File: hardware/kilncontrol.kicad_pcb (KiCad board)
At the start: 2 copper layers, 100 x 100 mm, 4 parts

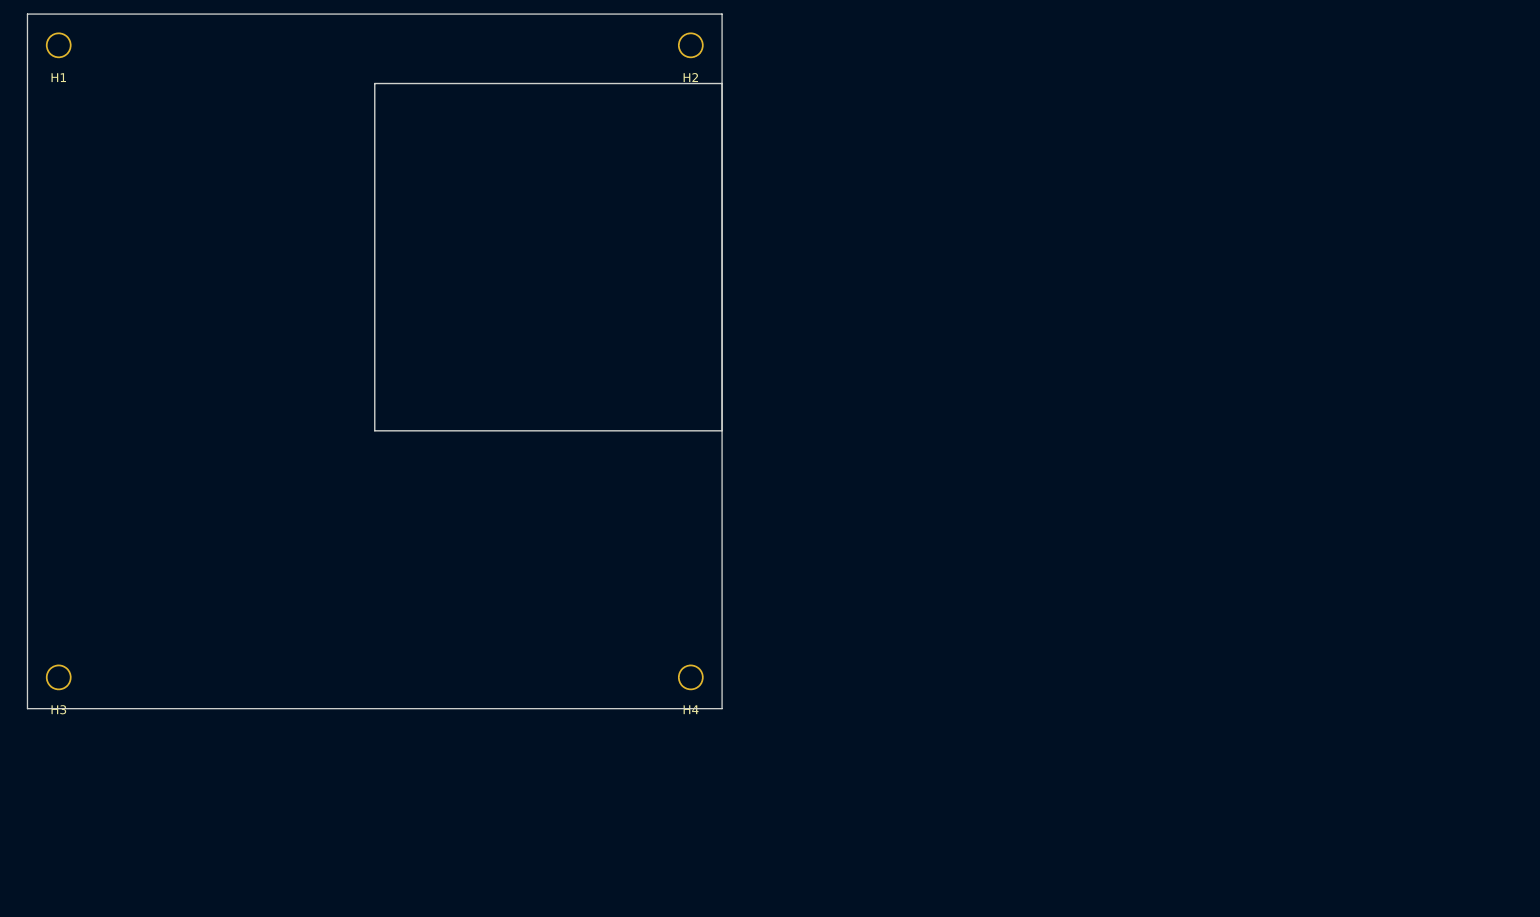
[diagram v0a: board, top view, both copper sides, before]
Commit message: Replace the external buzzer with an on-board one, shrink the test points
Buzzer
  J9, the screw terminal for an external buzzer, is replaced by BZ1 on the
  board: a TMB12A05, 5 V active (self-driving) magnetic buzzer, LCSC C96093.

  Active rather than passive: the 5 V-capable SMD passive part found on LCSC
  is rated 2.5-4.5 V and would be overdriven on the 5 V rail, and an active
  buzzer drops straight into the existing Q4 low-side driver and its flyback
  diode. No circuit change and no firmware change, because SR-20 asks the
  fault and completion alarms to be distinguishable by pattern, not by pitch,
  which kiln_alarm_pattern_t already does.

  This removes the auxiliary-relay output the old terminal also provided. The
  ALARM signal remains available at TP23 if an external annunciator is wanted
  later.

Test points
  All 33 change from TestPoint_THTPad_D2.0mm_Drill1.0mm to
  TestPoint_Pad_1.5x1.5mm: smaller, and SMD, so they sit on the top copper
  layer by construction rather than by layout discipline. The whole board can
  be probed without turning it over, and 33 drilled holes leave the board.

  A note on the sheet tells whoever does the placement not to move any test
  point to the bottom layer.

Requirements
  HR-09 now specifies an on-board buzzer rather than an alarm output capable
  of driving one. SR-20 reworded to match. New HR-19 (test points on the top
  layer only) and HR-20 (small pads, no drilled hole).

Housing
  The lid gains a perforated sound port above BZ1. A buzzer sealed inside the
  box is heavily muffled and SR-20 depends on the operator hearing it; a ring
  of 1.6 mm holes lets the sound out without leaving an opening large enough
  to drop debris onto the board.

Board
  Footprints imported from the schematic in KiCad since the last commit, and
  that import deleted the four M3 mounting holes, which are restored here.

  The imported footprints are STALE: they still carry J9, lack BZ1, and use
  the old 2 mm through-hole test pad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
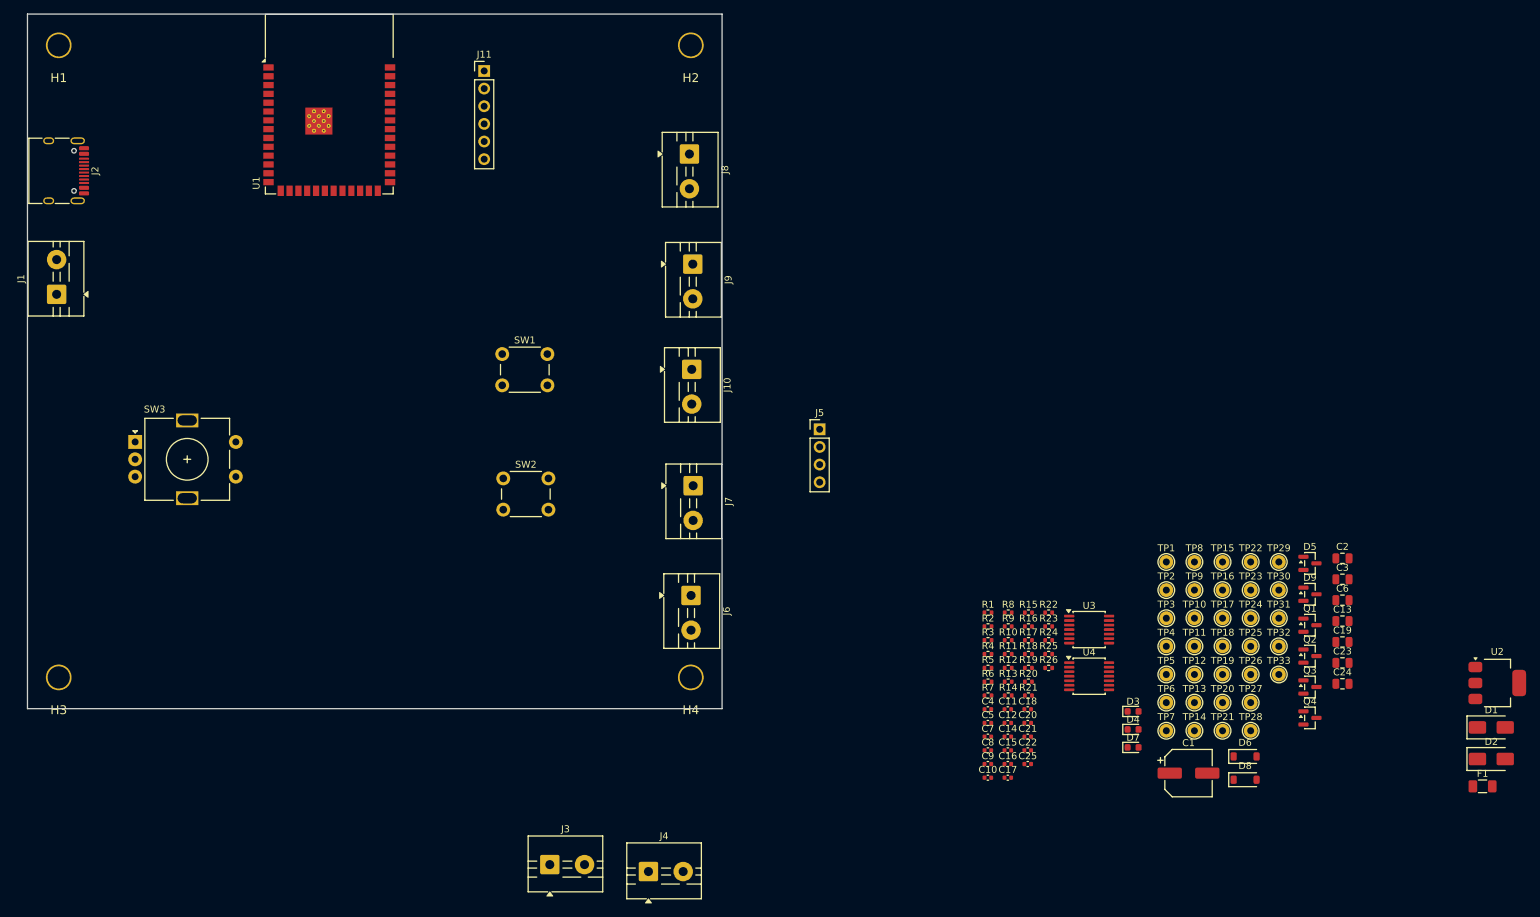
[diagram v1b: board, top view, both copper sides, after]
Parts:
- added C1: 100uF 16V, Capacitor_SMD:CP_Elec_6.3x7.7, F.Cu at (217.2, 149.3)
- added C10: 100pF, Capacitor_SMD:C_0402_1005Metric, F.Cu at (188.3, 149.9)
- added C11: 100nF, Capacitor_SMD:C_0402_1005Metric, F.Cu at (191.1, 140.1)
- added C12: 100nF, Capacitor_SMD:C_0402_1005Metric, F.Cu at (191.1, 142.1)
- added C13: 10uF, Capacitor_SMD:C_0805_2012Metric, F.Cu at (239.3, 127.4)
- added C14: 10nF, Capacitor_SMD:C_0402_1005Metric, F.Cu at (191.1, 144.0)
- added C15: 100pF, Capacitor_SMD:C_0402_1005Metric, F.Cu at (191.1, 146.0)
- added C16: 100pF, Capacitor_SMD:C_0402_1005Metric, F.Cu at (191.1, 148.0)
- added C17: 100nF, Capacitor_SMD:C_0402_1005Metric, F.Cu at (191.1, 149.9)
- added C18: 100nF, Capacitor_SMD:C_0402_1005Metric, F.Cu at (194.0, 140.1)
- added C19: 10uF, Capacitor_SMD:C_0805_2012Metric, F.Cu at (239.3, 130.4)
- added C2: 10uF, Capacitor_SMD:C_0805_2012Metric, F.Cu at (239.3, 118.4)
- added C20: 100nF, Capacitor_SMD:C_0402_1005Metric, F.Cu at (194.0, 142.1)
- added C21: 100nF, Capacitor_SMD:C_0402_1005Metric, F.Cu at (194.0, 144.0)
- added C22: 100nF, Capacitor_SMD:C_0402_1005Metric, F.Cu at (194.0, 146.0)
- added C23: 10uF, Capacitor_SMD:C_0805_2012Metric, F.Cu at (239.3, 133.4)
- added C24: 3.3uF, Capacitor_SMD:C_0805_2012Metric, F.Cu at (239.3, 136.4)
- added C25: 220nF, Capacitor_SMD:C_0402_1005Metric, F.Cu at (194.0, 148.0)
- added C3: 10uF, Capacitor_SMD:C_0805_2012Metric, F.Cu at (239.3, 121.4)
- added C4: 100nF, Capacitor_SMD:C_0402_1005Metric, F.Cu at (188.3, 140.1)
- added C5: 100nF, Capacitor_SMD:C_0402_1005Metric, F.Cu at (188.3, 142.1)
- added C6: 10uF, Capacitor_SMD:C_0805_2012Metric, F.Cu at (239.3, 124.4)
- added C7: 1uF, Capacitor_SMD:C_0402_1005Metric, F.Cu at (188.3, 144.0)
- added C8: 10nF, Capacitor_SMD:C_0402_1005Metric, F.Cu at (188.3, 146.0)
- added C9: 100pF, Capacitor_SMD:C_0402_1005Metric, F.Cu at (188.3, 148.0)
- added D1: SS34, Diode_SMD:D_SMA, F.Cu at (260.8, 142.7)
- added D2: SS34, Diode_SMD:D_SMA, F.Cu at (260.8, 147.2)
- added D3: SSR1, LED_SMD:LED_0603_1608Metric, F.Cu at (209.2, 140.4)
- added D4: SSR2, LED_SMD:LED_0603_1608Metric, F.Cu at (209.2, 143.0)
- added D5: BAT54S, Package_TO_SOT_SMD:SOT-23, F.Cu at (234.6, 119.1)
- added D6: 1N4148W, Diode_SMD:D_SOD-123, F.Cu at (225.3, 146.9)
- added D7: COIL, LED_SMD:LED_0603_1608Metric, F.Cu at (209.2, 145.6)
- added D8: 1N4148W, Diode_SMD:D_SOD-123, F.Cu at (225.3, 150.2)
- added D9: BAT54S, Package_TO_SOT_SMD:SOT-23, F.Cu at (234.6, 123.5)
- added F1: PTC 1.5A, Fuse:Fuse_1206_3216Metric, F.Cu at (259.5, 151.2)
- added J1: 5V DC IN, TerminalBlock:TerminalBlock_MaiXu_MX126-5.0-02P_1x02_P5.00mm, F.Cu at (54.2, 80.3)
- added J10: CT 30A/1V (opt), TerminalBlock:TerminalBlock_MaiXu_MX126-5.0-02P_1x02_P5.00mm, F.Cu at (145.6, 91.2)
- added J11: UART / EXPANSION, Connector_PinHeader_2.54mm:PinHeader_1x06_P2.54mm_Vertical, F.Cu at (115.8, 48.2)
- added J2: USB-C, Connector_USB:USB_C_Receptacle_HRO_TYPE-C-31-M-12, F.Cu at (54.1, 62.6)
- added J3: TC1 KILN (K), TerminalBlock:TerminalBlock_MaiXu_MX126-5.0-02P_1x02_P5.00mm, F.Cu at (125.2, 162.4)
- added J4: TC2 CASE (K), TerminalBlock:TerminalBlock_MaiXu_MX126-5.0-02P_1x02_P5.00mm, F.Cu at (139.4, 163.4)
- added J5: OLED 128x64 I2C, Connector_PinHeader_2.54mm:PinHeader_1x04_P2.54mm_Vertical, F.Cu at (164.1, 99.8)
- added J6: SSR1 CTRL, TerminalBlock:TerminalBlock_MaiXu_MX126-5.0-02P_1x02_P5.00mm, F.Cu at (145.5, 123.7)
- added J7: SSR2 CTRL (opt), TerminalBlock:TerminalBlock_MaiXu_MX126-5.0-02P_1x02_P5.00mm, F.Cu at (145.8, 107.9)
- added J8: CONTACTOR COIL 5V, TerminalBlock:TerminalBlock_MaiXu_MX126-5.0-02P_1x02_P5.00mm, F.Cu at (145.3, 60.1)
- added J9: BUZZER / AUX, TerminalBlock:TerminalBlock_MaiXu_MX126-5.0-02P_1x02_P5.00mm, F.Cu at (145.8, 76.0)
- added Q1: AO3400A, Package_TO_SOT_SMD:SOT-23, F.Cu at (234.6, 128.0)
- added Q2: AO3400A, Package_TO_SOT_SMD:SOT-23, F.Cu at (234.6, 132.4)
- added Q3: AO3400A, Package_TO_SOT_SMD:SOT-23, F.Cu at (234.6, 136.9)
- added Q4: AO3400A, Package_TO_SOT_SMD:SOT-23, F.Cu at (234.6, 141.3)
- added R1: 5.1k, Resistor_SMD:R_0402_1005Metric, F.Cu at (188.3, 126.2)
- added R10: 10k, Resistor_SMD:R_0402_1005Metric, F.Cu at (191.2, 130.2)
- added R11: 10k, Resistor_SMD:R_0402_1005Metric, F.Cu at (191.2, 132.1)
- added R12: 10k, Resistor_SMD:R_0402_1005Metric, F.Cu at (191.2, 134.1)
- added R13: 100R, Resistor_SMD:R_0402_1005Metric, F.Cu at (191.2, 136.1)
- added R14: 10k, Resistor_SMD:R_0402_1005Metric, F.Cu at (191.2, 138.1)
- added R15: 1k, Resistor_SMD:R_0402_1005Metric, F.Cu at (194.1, 126.2)
- added R16: 100R, Resistor_SMD:R_0402_1005Metric, F.Cu at (194.1, 128.2)
- added R17: 10k, Resistor_SMD:R_0402_1005Metric, F.Cu at (194.1, 130.2)
- added R18: 1k, Resistor_SMD:R_0402_1005Metric, F.Cu at (194.1, 132.1)
- added R19: 100R, Resistor_SMD:R_0402_1005Metric, F.Cu at (194.1, 134.1)
- added R2: 5.1k, Resistor_SMD:R_0402_1005Metric, F.Cu at (188.3, 128.2)
- added R20: 47k, Resistor_SMD:R_0402_1005Metric, F.Cu at (194.1, 136.1)
- added R21: 1k, Resistor_SMD:R_0402_1005Metric, F.Cu at (194.1, 138.1)
- added R22: 100R, Resistor_SMD:R_0402_1005Metric, F.Cu at (197.0, 126.2)
- added R23: 10k, Resistor_SMD:R_0402_1005Metric, F.Cu at (197.0, 128.2)
- added R24: 10k, Resistor_SMD:R_0402_1005Metric, F.Cu at (197.0, 130.2)
- added R25: 10k, Resistor_SMD:R_0402_1005Metric, F.Cu at (197.0, 132.1)
- added R26: 1k, Resistor_SMD:R_0402_1005Metric, F.Cu at (197.0, 134.1)
- added R3: 10k, Resistor_SMD:R_0402_1005Metric, F.Cu at (188.3, 130.2)
- added R4: 100R, Resistor_SMD:R_0402_1005Metric, F.Cu at (188.3, 132.1)
- added R5: 100R, Resistor_SMD:R_0402_1005Metric, F.Cu at (188.3, 134.1)
- added R6: 100R, Resistor_SMD:R_0402_1005Metric, F.Cu at (188.3, 136.1)
- added R7: 100R, Resistor_SMD:R_0402_1005Metric, F.Cu at (188.3, 138.1)
- added R8: 4.7k, Resistor_SMD:R_0402_1005Metric, F.Cu at (191.2, 126.2)
- added R9: 4.7k, Resistor_SMD:R_0402_1005Metric, F.Cu at (191.2, 128.2)
- added SW1: RESET, Button_Switch_THT:SW_PUSH_6mm_H5mm, F.Cu at (118.3, 89.0)
- added SW2: BOOT, Button_Switch_THT:SW_PUSH_6mm_H5mm, F.Cu at (118.5, 106.8)
- added SW3: ENCODER, Rotary_Encoder:RotaryEncoder_Alps_EC11E-Switch_Vertical_H20mm, F.Cu at (65.5, 101.6)
- added TP1: +5V, TestPoint:TestPoint_THTPad_D2.0mm_Drill1.0mm, F.Cu at (214.0, 118.9)
- added TP10: TC2_CS, TestPoint:TestPoint_THTPad_D2.0mm_Drill1.0mm, F.Cu at (218.0, 127.0)
- added TP11: TC1_DRDY, TestPoint:TestPoint_THTPad_D2.0mm_Drill1.0mm, F.Cu at (218.0, 131.0)
- added TP12: TC2_DRDY, TestPoint:TestPoint_THTPad_D2.0mm_Drill1.0mm, F.Cu at (218.0, 135.1)
- added TP13: TC1_FAULT, TestPoint:TestPoint_THTPad_D2.0mm_Drill1.0mm, F.Cu at (218.0, 139.1)
- added TP14: TC2_FAULT, TestPoint:TestPoint_THTPad_D2.0mm_Drill1.0mm, F.Cu at (218.0, 143.2)
- added TP15: I2C_SDA, TestPoint:TestPoint_THTPad_D2.0mm_Drill1.0mm, F.Cu at (222.1, 118.9)
- added TP16: I2C_SCL, TestPoint:TestPoint_THTPad_D2.0mm_Drill1.0mm, F.Cu at (222.1, 122.9)
- added TP17: SSR1, TestPoint:TestPoint_THTPad_D2.0mm_Drill1.0mm, F.Cu at (222.1, 127.0)
- added TP18: SSR2, TestPoint:TestPoint_THTPad_D2.0mm_Drill1.0mm, F.Cu at (222.1, 131.0)
- added TP19: HEAT_EN, TestPoint:TestPoint_THTPad_D2.0mm_Drill1.0mm, F.Cu at (222.1, 135.1)
- added TP2: +3V3, TestPoint:TestPoint_THTPad_D2.0mm_Drill1.0mm, F.Cu at (214.0, 122.9)
- added TP20: PUMP_NODE, TestPoint:TestPoint_THTPad_D2.0mm_Drill1.0mm, F.Cu at (222.1, 139.1)
- added TP21: HEAT_EN_DC, TestPoint:TestPoint_THTPad_D2.0mm_Drill1.0mm, F.Cu at (222.1, 143.2)
- added TP22: COIL_DRV, TestPoint:TestPoint_THTPad_D2.0mm_Drill1.0mm, F.Cu at (226.1, 118.9)
- added TP23: ALARM, TestPoint:TestPoint_THTPad_D2.0mm_Drill1.0mm, F.Cu at (226.1, 122.9)
- added TP24: ENC_A, TestPoint:TestPoint_THTPad_D2.0mm_Drill1.0mm, F.Cu at (226.1, 127.0)
- added TP25: ENC_B, TestPoint:TestPoint_THTPad_D2.0mm_Drill1.0mm, F.Cu at (226.1, 131.0)
- added TP26: ENC_BTN, TestPoint:TestPoint_THTPad_D2.0mm_Drill1.0mm, F.Cu at (226.1, 135.1)
- added TP27: TC1_P, TestPoint:TestPoint_THTPad_D2.0mm_Drill1.0mm, F.Cu at (226.1, 139.1)
- added TP28: TC1_N, TestPoint:TestPoint_THTPad_D2.0mm_Drill1.0mm, F.Cu at (226.1, 143.2)
- added TP29: TC2_P, TestPoint:TestPoint_THTPad_D2.0mm_Drill1.0mm, F.Cu at (230.2, 118.9)
- added TP3: GND, TestPoint:TestPoint_THTPad_D2.0mm_Drill1.0mm, F.Cu at (214.0, 127.0)
- added TP30: TC2_N, TestPoint:TestPoint_THTPad_D2.0mm_Drill1.0mm, F.Cu at (230.2, 122.9)
- added TP31: CURR_SENSE, TestPoint:TestPoint_THTPad_D2.0mm_Drill1.0mm, F.Cu at (230.2, 127.0)
- added TP32: MCU_EN, TestPoint:TestPoint_THTPad_D2.0mm_Drill1.0mm, F.Cu at (230.2, 131.0)
- added TP33: MCU_IO0, TestPoint:TestPoint_THTPad_D2.0mm_Drill1.0mm, F.Cu at (230.2, 135.1)
- added TP4: GND, TestPoint:TestPoint_THTPad_D2.0mm_Drill1.0mm, F.Cu at (214.0, 131.0)
- added TP5: VBUS, TestPoint:TestPoint_THTPad_D2.0mm_Drill1.0mm, F.Cu at (214.0, 135.1)
- added TP6: SPI_SCK, TestPoint:TestPoint_THTPad_D2.0mm_Drill1.0mm, F.Cu at (214.0, 139.1)
- added TP7: SPI_MOSI, TestPoint:TestPoint_THTPad_D2.0mm_Drill1.0mm, F.Cu at (214.0, 143.2)
- added TP8: SPI_MISO, TestPoint:TestPoint_THTPad_D2.0mm_Drill1.0mm, F.Cu at (218.0, 118.9)
- added TP9: TC1_CS, TestPoint:TestPoint_THTPad_D2.0mm_Drill1.0mm, F.Cu at (218.0, 122.9)
- added U1: ESP32-S3-WROOM-1, RF_Module:ESP32-S3-WROOM-1, F.Cu at (93.5, 52.9)
- added U2: AMS1117-3.3, Package_TO_SOT_SMD:SOT-223-3_TabPin2, F.Cu at (261.6, 136.3)
- added U3: MAX31856, Package_SO:TSSOP-14_4.4x5mm_P0.65mm, F.Cu at (202.8, 128.6)
- added U4: MAX31856, Package_SO:TSSOP-14_4.4x5mm_P0.65mm, F.Cu at (202.8, 135.3)
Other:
- outline, holes or cut-outs redrawn

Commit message: hw: interrupt the contactor coil from the fault pins and the lid
The coil circuit becomes a series chain of four independent interrupts, three
of which need no firmware at all:

  +5V -[J9 lid, NC]- J8 [COIL] -COIL_DRV- Q3 -COIL_RTN1- Q6 -COIL_RTN2- Q5 - GND
                                       charge pump    TC1 FAULT    TC2 FAULT

Q5 and Q6 are AO3400A with 10k gate pull-ups (R28, R29) to +3V3. J9's lid
contacts move into the coil supply so they carry coil current directly rather
than only being sensed. LID_SENSE brings the node back to IO38 through an
R30/R31 10k/18k divider, 5 V to 3.21 V, so SR-31 can still see the door; IO38
because IO2, IO3, IO45 and IO46 are strapping pins and HR-08 rules them out.

Each FAULT output drives its own MOSFET rather than being wire-ANDed onto one
node. Wire-ANDing would have merged TC1_FAULT and TC2_FAULT into a single net
and cost the per-device test points; a MOSFET each keeps both names, both
probe points, and buys two independent interrupts for the price of one part.

The flyback diode was on the wrong side of the new contact. D6's cathode went
to raw +5V, which the lid now bypasses, so opening the lid would have left the
coil with no freewheel path and put the inductive kick across the switch
contacts. Moved to the LID_SWITCH node so the loop is across the coil itself.
HR-25 records it so it cannot be undone by accident.

What this interlock is not: the FAULT outputs are open-drain, so an unpowered
or absent front end leaves its transistor on and the path closed, and the
MAX31856 detects an open circuit only once its fault mask is configured. They
interrupt on faults the device actively reports. SR-04 in firmware remains the
cover for a dead or unconfigured front end. The lid contact carries no such
caveat, being a contact in the circuit.

ERC unchanged at one error, the known U3 SDO output-output false positive.
Every net confirmed by query rather than by eye.

This commit also carries PCB layout and project state that w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
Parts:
- removed H1, H2, H3, H4: MountingHole, MountingHole:MountingHole_3.2mm
- removed J9: BUZZER / AUX, TerminalBlock:TerminalBlock_MaiXu_MX126-5.0-02P_1x02_P5.00mm
- added BZ1: TMB12A05 5V, Buzzer_Beeper:Buzzer_12x9.5RM7.6, F.Cu at (124.8, 50.4)
- TP1, TP10, TP11, TP12, TP13, TP14, TP15, TP16, TP17, TP18, TP19, TP2, TP20, TP21, TP22, TP23, TP24, TP25, TP26, TP27, TP28, TP29, TP3, TP30, TP31, TP32, TP33, TP4, TP5, TP6, TP7, TP8, TP9: footprint TestPoint:TestPoint_THTPad_D2.0mm_Drill1.0mm -> TestPoint:TestPoint_Pad_1.5x1.5mm
- moved U2 211.3 mm to (67.5, 52.8)
- moved TP1 209.8 mm to (26.0, 25.6)
- moved TP2 207.9 mm to (26.0, 34.0)
- moved F1 206.2 mm to (67.1, 76.9)
- moved D1 206.2 mm to (68.4, 68.4)
- moved D2 206.2 mm to (68.4, 73.0)
- moved TP3 206.1 mm to (26.0, 42.4)
- moved TP19 205.9 mm to (33.0, 53.4)
- moved TP4 204.4 mm to (26.0, 50.8)
- moved TP20 204.3 mm to (33.0, 61.8)
- moved TP5 202.7 mm to (26.0, 59.2)
- moved TP21 202.7 mm to (33.0, 70.2)
- moved TP6 201.1 mm to (26.0, 67.6)
- moved TP33 200.4 mm to (33.0, 171.0)
- moved TP32 199.7 mm to (33.0, 162.6)
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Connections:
- net /+5V renamed +5V
- net /ALARM_G renamed Net-(Q4-G)
- net /GND renamed GND
- net /PUMP_DRV renamed Net-(C23-Pad1)
- net /SSR1_G renamed Net-(Q1-G)
- net /SSR1_LED_A renamed Net-(D3-A)
- net /SSR2_G renamed Net-(Q2-G)
- net /SSR2_LED_A renamed Net-(D4-A)
- C11 pad 1: /+3V3 -> +3.3V
- C12 pad 1: /+3V3 -> +3.3V
- C13 pad 1: /+3V3 -> +3.3V
- C17 pad 1: /+3V3 -> +3.3V
- C18 pad 1: /+3V3 -> +3.3V
- C19 pad 1: /+3V3 -> +3.3V
- C3 pad 1: /+3V3 -> +3.3V
- C4 pad 1: /+3V3 -> +3.3V
- C5 pad 1: /+3V3 -> +3.3V
- C6 pad 1: /+3V3 -> +3.3V
- D9 pad 2: /+3V3 -> +3.3V
- J11 pad 2: /+3V3 -> +3.3V
- J5 pad 2: /+3V3 -> +3.3V
- R10 pad 1: /+3V3 -> +3.3V
- R11 pad 1: /+3V3 -> +3.3V
- R12 pad 1: /+3V3 -> +3.3V
- R24 pad 1: /+3V3 -> +3.3V
- R8 pad 1: /+3V3 -> +3.3V
- R9 pad 1: /+3V3 -> +3.3V
- U1 pad 2: /+3V3 -> +3.3V
- U2 pad 2: /+3V3 -> +3.3V
- U3 pad 5: /+3V3 -> +3.3V
- U3 pad 8: /+3V3 -> +3.3V
- U4 pad 5: /+3V3 -> +3.3V
- U4 pad 8: /+3V3 -> +3.3V
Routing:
- added copper zone on B.Cu, net GND
- added copper zone on F.Cu, net GND

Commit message: hw: pull the PCB up to the schematic, and start placement
The board had not been updated since section K went into the schematic --
update_pcb_from_schematic had never been run against it, which the tasklist
has been recording as an open item. It is run now, so the interlock chain's
parts exist on the board: J9, Q5, Q6 and R28 to R31 arrive as footprints, and
D4, J7, Q2 and R16 to R18 leave with the symbols they belonged to. R27 goes
from the schematic as well.

Placement is started, not finished: 74 footprints are repositioned, and
nothing is routed. There are no tracks and no vias on the board at all, and
the sixteen zones are untouched, so this is the arrangement pass and the
copper comes after it.

Both files are also written out in KiCad's current s-expression format, which
is why the diffs are far larger than the edits. Almost none of that is
whitespace -- `git diff -w` barely shrinks it -- so it is a genuine
restructuring of the files by the editor rather than a reflow, and it is not
worth trying to separate from the real changes.
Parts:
- removed D4: SSR2, LED_SMD:LED_0603_1608Metric
- removed J7: SSR2 CTRL (opt), TerminalBlock:TerminalBlock_MaiXu_MX126-5.0-02P_1x02_P5.00mm
- removed Q2: AO3400A, Package_TO_SOT_SMD:SOT-23
- removed R16: 100R, Resistor_SMD:R_0402_1005Metric
- removed R17: 10k, Resistor_SMD:R_0402_1005Metric
- removed R18: 1k, Resistor_SMD:R_0402_1005Metric
- added J9: LID SWITCH, TerminalBlock:TerminalBlock_MaiXu_MX126-5.0-02P_1x02_P5.00mm, F.Cu at (146.0, 95.5)
- added Q5: AO3400A, Package_TO_SOT_SMD:SOT-23, F.Cu at (122.4, 61.3)
- added Q6: AO3400A, Package_TO_SOT_SMD:SOT-23, F.Cu at (126.7, 61.3)
- added R28: 10k, Resistor_SMD:R_0402_1005Metric, F.Cu at (124.0, 59.8)
- added R29: 10k, Resistor_SMD:R_0402_1005Metric, F.Cu at (119.8, 59.7)
- added R30: 10k, Resistor_SMD:R_0402_1005Metric, F.Cu at (138.2, 56.5)
- added R31: 18k, Resistor_SMD:R_0402_1005Metric, F.Cu at (138.2, 54.5)
- SW1: moved to B.Cu
- moved C4 153.8 mm to (61.2, 57.0), turned to -90 degrees
- moved C5 147.1 mm to (76.5, 48.2), turned to 90 degrees
- moved R1 145.9 mm to (60.7, 61.2)
- moved R2 145.5 mm to (60.7, 64.2)
- moved R10 145.0 mm to (55.3, 93.8)
- moved R11 143.5 mm to (53.8, 115.5)
- moved C7 142.2 mm to (76.0, 59.2)
- moved R3 139.6 mm to (75.8, 50.5)
- moved Q4 130.8 mm to (110.9, 49.0)
- moved R12 127.0 mm to (71.5, 108.2), turned to 180 degrees
- moved C24 120.0 mm to (127.8, 57.5), turned to 90 degrees
- moved R22 119.6 mm to (108.2, 47.5), turned to -90 degrees
- moved R23 119.6 mm to (108.2, 49.5), turned to -90 degrees
- moved Q3 118.9 mm to (130.9, 61.3)
- moved C23 118.7 mm to (134.0, 57.5), turned to -90 degrees
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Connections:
- net /COIL_LED_A renamed Net-(D7-A)
- D6 pad 1: +5V -> /LID_SWITCH
- J8 pad 1: +5V -> /LID_SWITCH
- Q3 pad 2: GND -> /COIL_RTN1
- R3 pad 1: /+3V3 -> +3.3V
- SW1 pad 1: /MCU_EN -> GND
- SW1 pad 2: GND -> /MCU_EN
- SW2 pad 1: /MCU_IO0 -> GND
- SW2 pad 2: GND -> /MCU_IO0
- U1 pad 31: unconnected-(U1-IO38-Pad31) -> /LID_SENSE

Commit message: hw: another pass over the placement
94 of the 117 footprints move. Nothing is added or removed, the schematic is
unchanged in substance (256 wires, 49 junctions, 123 labels before and after,
reordered by the editor on save), and the board is still unrouted: zero tracks,
zero vias, the sixteen zones untouched.

So this is the arrangement continuing, not the copper starting. A23 and K4
still hold.
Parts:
- moved TP17 152.3 mm to (138.0, 56.8)
- moved TP31 131.6 mm to (140.0, 77.5)
- moved TP18 125.8 mm to (75.5, 52.8)
- moved TP33 122.2 mm to (117.8, 83.0)
- moved C21 119.0 mm to (56.7, 88.8)
- moved C22 115.6 mm to (56.8, 87.8)
- moved TP30 113.7 mm to (139.7, 106.5)
- moved TP28 112.4 mm to (140.0, 94.5)
- moved TP32 109.2 mm to (107.8, 83.0)
- moved TP29 109.0 mm to (139.7, 115.2)
- moved TP27 108.3 mm to (140.0, 103.8)
- moved C20 107.6 mm to (56.7, 89.8)
- moved TP20 106.2 mm to (137.2, 41.8)
- moved TP14 104.1 mm to (127.5, 111.8)
- moved TP13 103.0 mm to (125.7, 100.5)
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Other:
- outline, holes or cut-outs redrawn
